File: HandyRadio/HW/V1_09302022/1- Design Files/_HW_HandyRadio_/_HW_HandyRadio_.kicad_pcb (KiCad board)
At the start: 4 copper layers, 74.9 x 74.9 mm, 170 parts, among them J1 MHDR_4POS_1ROW, J2 RECEP_6POS_1ROW, J3 XH_CONN_2POS_R/A, J4 USB_uAB_RECEP, J5 XH_CONN_2POS_R/A, J6 MHDR_2POS_VERT, K1 DPDT_RELAY, Q1 IRF7401TRPBF, Q2 MMUN2215LT1G, SW1 SPST_NO_RA, SW2 SPST_NO_RA, SW3 SPST_NO_RA, U1 PIC16F15223, U2 IR_REC_38KHz, U3 PAM8302AASCR, U4 MCP73831, U5 AP7361EA, U6 R1211N002B, U7 MIC5365-3.3, U8 EGUARD0502A, U9 SI4735-D60-GU

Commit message: IT'S ALMOST GOOD FOR RELEASE, schematic should be checked and a double check on routing
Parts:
- H2, H3, H4, H5: footprint MountingHole:MountingHole_3.2mm_M3 -> _HW_HandyRadio_Footprint:MountingHole_3.2mm_M3
- moved H4 3.80 mm to (250.2, 176.4)
- moved H5 3.43 mm to (183.3, 176.5)
- moved H3 3.43 mm to (250.6, 109.2)
- moved H2 3.41 mm to (183.3, 109.2)
- moved R37 0.66 mm to (240.4, 137.2)
- moved R2 0.63 mm to (250.6, 121.6)
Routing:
- net GND: track 198.4 -> 206.7 mm
- net /BLOCK DIAGRAM/MCU, RTC, OLED, PB, LED/BATT_STAT: track 79.1 -> 87.2 mm
- net /BLOCK DIAGRAM/MCU, RTC, OLED, PB, LED/PB_1: track 37.2 -> 45.2 mm
- net /BLOCK DIAGRAM/MCU, RTC, OLED, PB, LED/~{FM}/SW_SEL: track 47.0 -> 51.5 mm
- net /BLOCK DIAGRAM/MCU, RTC, OLED, PB, LED/IR_INPUT: track 49.7 -> 52.7 mm
- net /BLOCK DIAGRAM/MCU, RTC, OLED, PB, LED/ICSPCLK: track 76.8 -> 75.8 mm
- net Net-(J1-Pad4): track 3.11 -> 3.75 mm
- added copper zone on B.Cu, net GND
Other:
- board text added: "! DO NOT TOUCH !"
- board text added: "(C) 2022 Siavash Taher Parvar ALL RIGHTS RESERVED"
- board text added: "+ -"
- board text added: "+3.7V BATT"
- board text added: "+SPK -SPK"
- board text added: "8OHM SPK"
- board text added: "@Mend0z0"
- board text added: "AM ANT"
- board text added: "GND ICSPCLK ICSPDAT VCC"
- board text added: "Handy Radio Supported band AM/FM/SW/LW"
- board text added: "IR GND VCC"
- board text added: "M3"
- board text added: "Released Date: Nov 2nd, 2022"
- board text added: "To my professors that I liked to present this project while they were alive. GOD BLESS YOU, RIP! Prof. Nina Jagaric (RF Class) Prof. Kam Pui Tang (MCU Class) Fall 2022, Centennial College"
- board text added: "Version/Revsion: V1I1"
- board text added: "X RST SDA SCL +3V3 GND"

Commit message: some modification
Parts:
- removed DIS1: OLED, _HW_HandyRadio_Footprint:OLED 1.3INCH
- added DIS601: OLED, _HW_HandyRadio_Footprint:OLED 1.3INCH, F.Cu at (202.7, 126.1)
- added R512: 16K5R, Resistor_SMD:R_0805_2012Metric_Pad1.20x1.40mm_HandSolder, F.Cu at (173.2, 145.3)
- added REF**: Logo, _HW_HandyRadio_Footprint:Logo, F.Cu at (239.6, 124.7)
- added TP506: TPC, TestPoint:TestPoint_Pad_D1.5mm, F.Cu at (169.3, 138.0)
- renumbered ANT2 to ANT801, C1 to C301, C2 to C302, C3 to C303, C4 to C304, C5 to C305, C6 to C306, C7 to C307, C8 to C308, C9 to C309, C10 to C310, C11 to C311, C12 to C312, C13 to C313, C14 to C314, C15 to C315, C16 to C316, C17 to C401, C18 to C402, C19 to C403, C20 to C404, C21 to C405, C22 to C406, C23 to C407, C24 to C501, C25 to C502, C26 to C503, C27 to C504, C28 to C505, C29 to C506, C30 to C507, C31 to C508, C32 to C509, C33 to C510, C34 to C511, C35 to C512, C36 to C513, C37 to C514, C38 to C515, C39 to C516, C40 to C517, C41 to C518, C42 to C519, C43 to C520, C44 to C521, C45 to C522, C46 to C523, C47 to C524, C48 to C525, C49 to C526, C50 to C527, C51 to C528, C52 to C801, C53 to C802, C54 to C803, C55 to C804, C56 to C805, C57 to C806, C58 to C807, C59 to C808, C60 to C809, C61 to C810, C62 to C811, C63 to C812, C64 to C813, C65 to C814, C66 to C815, C67 to C816, C68 to C817, C69 to C818, C70 to C819, D1 to D301, D2 to D501, EC1 to EC501, EC2 to EC502, EC3 to EC503, EC4 to EC801, EC5 to EC802, EC6 to EC803, H2 to H602, H3 to H603, H4 to H604, H5 to H605, J1 to J301, J2 to J302, J3 to J401, J4 to J501, J5 to J502, J6 to J801, K1 to K801, L1 to L501, L2 to L801, L3 to L802, L4 to L803, L5 to L804, Q1 to Q501, Q2 to Q801, R1 to R301, R2 to R302, R3 to R303, R4 to R304, R5 to R305, R6 to R306, R7 to R307, R8 to R308, R9 to R309, R10 to R310, R11 to R311, R12 to R312, R13 to R313, R14 to R314, R15 to R315, R16 to R316, R17 to R401, R18 to R402, R19 to R403, R20 to R501, R21 to R502, R22 to R503, R23 to R504, R24 to R505, R25 to R506, R26 to R507, R27 to R508, R28 to R509, R29 to R510, R30 to R511, R32 to R801, R33 to R802, R34 to R803, R35 to R804, R36 to R805, R37 to R806, R38 to R807, R39 to R808, SW1 to SW301, SW2 to SW302, SW3 to SW303, TP1 to TP301, TP2 to TP302, TP3 to TP303, TP4 to TP304, TP5 to TP305, TP6 to TP306, TP7 to TP307, TP8 to TP308, TP9 to TP309, TP10 to TP310, TP11 to TP501, TP12 to TP502, TP13 to TP503, TP14 to TP504, TP15 to TP505, TP17 to TP507, TP18 to TP508, TP19 to TP509, TP20 to TP801, TP21 to TP802, U1 to U301, U2 to U302, U3 to U401, U4 to U501, U5 to U502, U6 to U503, U7 to U504, U8 to U801, U9 to U802
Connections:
- C521 pad 1: Net-(C44-Pad1) -> Net-(C521-Pad1)
- R506 pad 2: Net-(C44-Pad1) -> Net-(C521-Pad1)
- R508 pad 2: Net-(C44-Pad1) -> Net-(C521-Pad1)
- R511 pad 1: Net-(C44-Pad1) -> Net-(C521-Pad1)
- TP505 pad 1: Net-(C44-Pad1) -> Net-(C521-Pad1)
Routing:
- net Net-(C521-Pad1): track 0.00 -> 17.7 mm, vias 0 -> 1
- net Net-(C44-Pad1): track 17.7 -> 0.00 mm, vias 1 -> 0
- net GND: track 206.7 -> 202.2 mm, vias 98 -> 96
- net +3V3: track 95.9 -> 97.8 mm
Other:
- board text removed: "@Mend0z0"

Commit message: Serious changes in placement
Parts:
- removed R31: 16KR5, Resistor_SMD:R_0805_2012Metric_Pad1.20x1.40mm_HandSolder
- C308, C313, C316, C401, C402, C403, C502, C503, C504, C505, C506, C510, C511, C512, C514, C517, C518, C519, C520, C522, C524, C801, C802, C803, C806, C807, C810, C813, C818, C819, EC801, EC802, EC803, Q801, R309, R310, R312, R314, R315, R316, R502, R505, R508, R509, R510, R807, R808: moved to F.Cu
- moved R512 28.0 mm to (197.0, 160.0), turned to 180 degrees
- moved TP506 27.1 mm to (196.1, 141.9)
- moved R807 25.5 mm to (247.8, 135.0), turned to 180 degrees
- moved R808 24.2 mm to (251.9, 135.0), turned to 0 degrees
- moved C819 18.4 mm to (247.8, 137.2), turned to 0 degrees
- moved C818 16.7 mm to (251.9, 137.2), turned to 180 degrees
- moved R510 12.3 mm to (201.9, 148.8)
- moved C313 11.7 mm to (220.4, 115.8), turned to 0 degrees
- moved R312 11.7 mm to (224.4, 115.8), turned to 180 degrees
- moved C807 11.6 mm to (230.6, 162.3), turned to 0 degrees
- moved Q801 10.8 mm to (226.3, 166.5), turned to 0 degrees
- moved C524 10.1 mm to (208.3, 113.9), turned to 180 degrees
- moved TP307 9.60 mm to (214.0, 175.3)
- moved TP310 9.60 mm to (214.0, 177.8)
- moved C403 9.28 mm to (201.1, 165.8), turned to 0 degrees
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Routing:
- net GND: track 202.2 -> 17.7 mm, vias 96 -> 11
- net +5V: track 65.5 -> 0.00 mm, vias 26 -> 0
- net +3V3: track 97.8 -> 33.6 mm, vias 30 -> 5
- net /BLOCK DIAGRAM/MCU, RTC, OLED, PB, LED/BATT_STAT: track 87.2 -> 54.3 mm, vias 2 -> 0
- net +6V: track 30.0 -> 0.00 mm, vias 13 -> 0
- net +BATT: track 24.5 -> 0.00 mm, vias 12 -> 3
- net /BLOCK DIAGRAM/RF RECEIVER/~{RST}: track 22.2 -> 0.00 mm
- net Net-(C809-Pad1): track 19.5 -> 0.00 mm, vias 2 -> 0
- net /BLOCK DIAGRAM/RF RECEIVER/~{SEN}: track 19.1 -> 0.00 mm
- net /BLOCK DIAGRAM/MCU, RTC, OLED, PB, LED/~{FM}/SW_SEL: track 51.5 -> 32.7 mm, vias 2 -> 1
- net Net-(R502-Pad2): track 18.5 -> 0.00 mm, vias 1 -> 0
- net Net-(C521-Pad1): track 17.7 -> 0.00 mm, vias 1 -> 0
- net /BLOCK DIAGRAM/RF RECEIVER/SCLK: track 16.9 -> 0.00 mm
- net /BLOCK DIAGRAM/MCU, RTC, OLED, PB, LED/SI47_CLK: track 28.8 -> 14.1 mm
- net /BLOCK DIAGRAM/RF RECEIVER/SDIO: track 14.3 -> 0.00 mm
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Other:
- board size 74.9 x 74.9 mm -> 75 x 75 mm
- board text removed: "M3"

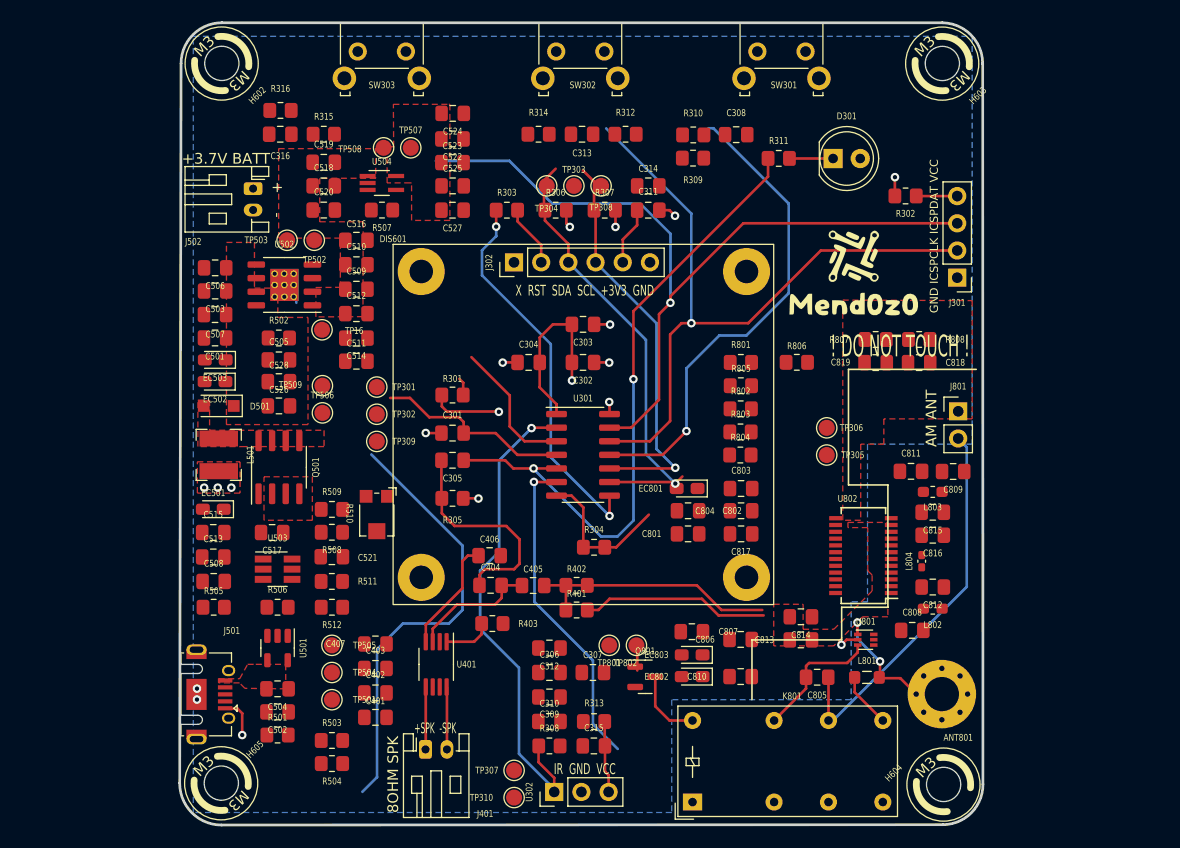
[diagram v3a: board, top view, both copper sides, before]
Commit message: replacement almost done, but routing left
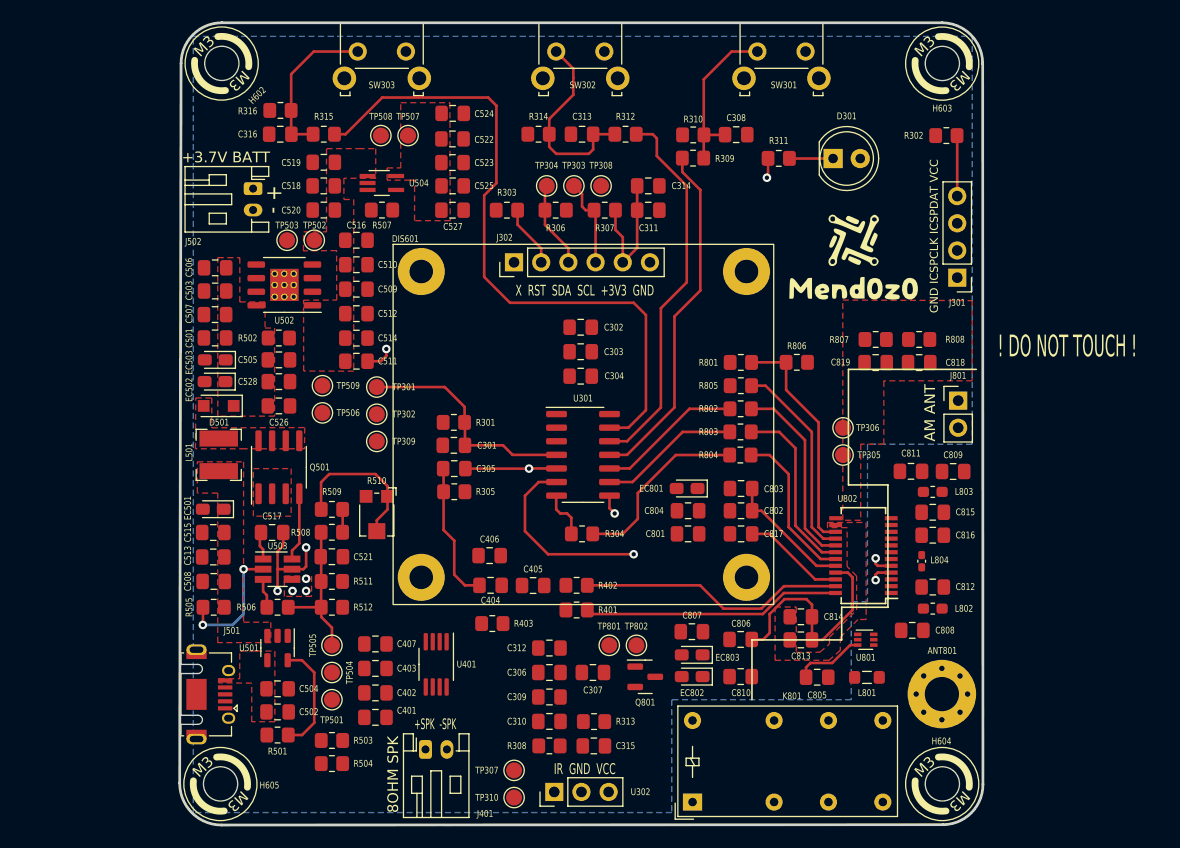
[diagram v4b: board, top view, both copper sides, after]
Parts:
- removed REF**: Logo, _HW_HandyRadio_Footprint:Logo
- removed TP16: TPC, TestPoint:TestPoint_Pad_D1.5mm
- added LBL602: Mend0z0_LOGO, _HW_HandyRadio_Footprint:Logo, F.Cu at (239.5, 123.2)
- moved R302 6.81 mm to (254.4, 116.0)
- moved C304 5.03 mm to (220.3, 138.4), turned to 180 degrees
- moved C302 3.29 mm to (220.3, 133.9)
- moved C303 2.57 mm to (220.3, 136.2)
- moved R301 2.56 mm to (208.4, 142.8)
- moved R304 1.68 mm to (220.4, 153.2)
- moved TP305 1.52 mm to (244.8, 145.8)
- moved TP306 1.52 mm to (244.8, 143.3)
- moved TP507 1.17 mm to (204.1, 116.0)
- moved TP508 1.17 mm to (201.6, 116.0)
- moved C301 1.15 mm to (208.4, 144.9)
- moved J801 1.00 mm to (255.5, 140.7)
- moved C305 0.80 mm to (208.4, 147.1)
- moved R305 0.64 mm to (208.4, 149.2)
- moved H604 0.13 mm to (251.6, 179.0)
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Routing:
- net /BLOCK DIAGRAM/MCU, RTC, OLED, PB, LED/BATT_STAT: track 54.3 -> 0.00 mm
- net /BLOCK DIAGRAM/MCU, RTC, OLED, PB, LED/LED_IND: track 60.7 -> 10.4 mm
- net /BLOCK DIAGRAM/MCU, RTC, OLED, PB, LED/IR_INPUT: track 46.1 -> 0.00 mm, vias 1 -> 0
- net Net-(C805-Pad1): track 36.4 -> 0.00 mm
- net Net-(R303-Pad1): track 35.9 -> 1.87 mm, vias 2 -> 1
- net /BLOCK DIAGRAM/MCU, RTC, OLED, PB, LED/ICSPCLK: track 66.0 -> 35.5 mm, vias 1 -> 0
- net /BLOCK DIAGRAM/RF RECEIVER/~{RST}: track 0.00 -> 21.7 mm
- net +5V: track 0.00 -> 21.5 mm
- net /BLOCK DIAGRAM/MCU, RTC, OLED, PB, LED/I2C_SDA: track 42.1 -> 21.3 mm, vias 1 -> 0
- net /BLOCK DIAGRAM/RF RECEIVER/~{SEN}: track 0.00 -> 19.0 mm
- net Net-(C313-Pad2): track 0.00 -> 18.5 mm
- net /BLOCK DIAGRAM/RF RECEIVER/SCLK: track 0.00 -> 18.0 mm
- net /BLOCK DIAGRAM/RF RECEIVER/SDIO: track 0.00 -> 16.8 mm
- net /BLOCK DIAGRAM/MCU, RTC, OLED, PB, LED/I2C_SCL: track 37.6 -> 22.0 mm, vias 1 -> 0
- net Net-(C308-Pad2): track 0.00 -> 15.4 mm
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
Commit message: routing on progress
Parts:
- moved C316 43.3 mm to (235.2, 120.7), turned to 180 degrees
- moved R315 35.4 mm to (231.3, 120.7), turned to 180 degrees
- moved C308 19.1 mm to (235.2, 135.0)
- moved R309 16.9 mm to (231.3, 135.0)
- moved C313 16.5 mm to (235.2, 123.0), turned to 180 degrees
- moved R312 9.88 mm to (231.3, 123.0), turned to 0 degrees
- moved R310 8.47 mm to (239.2, 115.2)
- moved R311 4.85 mm to (239.3, 122.9)
- moved R316 4.31 mm to (196.3, 115.1), turned to 0 degrees
- moved R314 4.15 mm to (220.4, 115.1)
- moved C809 3.07 mm to (253.1, 144.9), turned to 0 degrees
- moved TP305 2.95 mm to (244.8, 142.9), turned to -90 degrees
- moved TP306 2.13 mm to (244.8, 145.4), turned to -90 degrees
- moved C811 2.04 mm to (253.1, 147.1)
- moved U504 0.87 mm to (201.7, 119.5)
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- renumbered EC501 to TC501, EC502 to TC502, EC503 to TC503, EC801 to TC801, EC802 to TC802, EC803 to TC803
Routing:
- net Net-(C805-Pad1): track 0.00 -> 38.9 mm
- net Net-(C316-Pad2): track 14.7 -> 52.4 mm, vias 0 -> 1
- net Net-(C308-Pad2): track 15.4 -> 49.8 mm
- net GND: track 12.8 -> 45.4 mm, vias 3 -> 29
- net +3V3: track 24.9 -> 50.8 mm, vias 0 -> 24
- net Net-(C809-Pad1): track 0.00 -> 23.7 mm, vias 0 -> 2
- net Net-(C313-Pad2): track 18.5 -> 41.2 mm, vias 0 -> 1
- net /BLOCK DIAGRAM/MCU, RTC, OLED, PB, LED/ICSPCLK: track 35.5 -> 56.1 mm, vias 0 -> 1
- net /BLOCK DIAGRAM/MCU, RTC, OLED, PB, LED/PB_1: track 32.9 -> 14.8 mm
- net Net-(ANT801-Pad1): track 0.00 -> 16.9 mm, vias 0 -> 1
- net /BLOCK DIAGRAM/MCU, RTC, OLED, PB, LED/BATT_STAT: track 0.00 -> 14.3 mm
- net Net-(C404-Pad2): track 0.00 -> 12.2 mm
- net Net-(C406-Pad2): track 0.00 -> 10.7 mm
- net /BLOCK DIAGRAM/MCU, RTC, OLED, PB, LED/IR_INPUT: track 0.00 -> 8.87 mm
- net /BLOCK DIAGRAM/MCU, RTC, OLED, PB, LED/~{FM}/SW_SEL: track 17.8 -> 26.6 mm, vias 1 -> 2
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- added copper zone on B.Cu, net +3V3
- added copper zone on B.Cu, net +5V
- added copper zone on B.Cu, net +BATT
- added copper zone on In2.Cu, net GND
- removed copper zone on In2.Cu, net +3V3
- removed copper zone on In2.Cu, net +5V
- removed copper zone on In2.Cu, net +6V
- removed copper zone on In2.Cu, net +BATT
- removed copper zone on B.Cu, net GND
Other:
- board text added: "Handy Radio Supported bands AM/FM/SW/LW"
- board text removed: "Handy Radio Supported band AM/FM/SW/LW"

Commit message: routing has been almost done
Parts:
- moved R402 2.82 mm to (220.4, 155.2)
- moved R401 2.34 mm to (220.4, 158.0)
- moved TP301 1.14 mm to (201.2, 140.6)
- moved TP302 1.14 mm to (201.2, 143.1)
- moved TP309 1.14 mm to (201.2, 145.7)
- moved SW301 0.52 mm to (239.2, 110.3)
- moved SW302 0.52 mm to (220.4, 110.3)
- moved SW303 0.52 mm to (201.9, 110.3)
- moved TP501 0.10 mm to (197.1, 168.7)
- moved TP504 0.10 mm to (197.1, 166.1)
- moved TP505 0.10 mm to (197.1, 163.6)
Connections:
- R304 pad 1: /BLOCK DIAGRAM/MCU, RTC, OLED, PB, LED/SI47_CLK -> Net-(R304-Pad1)
- U301 pad 7: /BLOCK DIAGRAM/MCU, RTC, OLED, PB, LED/SI47_CLK -> Net-(R304-Pad1)
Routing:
- net /BLOCK DIAGRAM/MCU, RTC, OLED, PB, LED/IR_INPUT: track 8.87 -> 86.5 mm, vias 0 -> 1
- net GND: track 45.4 -> 106.1 mm, vias 29 -> 62
- net /BLOCK DIAGRAM/MCU, RTC, OLED, PB, LED/LED_IND: track 8.52 -> 68.3 mm, vias 1 -> 2
- net /BLOCK DIAGRAM/MCU, RTC, OLED, PB, LED/BATT_STAT: track 14.3 -> 63.4 mm, vias 0 -> 2
- net Net-(R303-Pad1): track 1.87 -> 35.3 mm, vias 1 -> 2
- net +6V: track 0.00 -> 31.8 mm, vias 0 -> 2
- net /BLOCK DIAGRAM/RF RECEIVER/GPO2: track 2.04 -> 31.5 mm, vias 1 -> 2
- net /BLOCK DIAGRAM/RF RECEIVER/GPO1: track 2.04 -> 28.6 mm, vias 1 -> 2
- net +BATT: track 4.61 -> 28.7 mm, vias 13 -> 15
- net /BLOCK DIAGRAM/MCU, RTC, OLED, PB, LED/SI47_CLK: track 21.8 -> 35.6 mm, vias 0 -> 2
- net Net-(R304-Pad1): track 0.00 -> 4.77 mm
- net /BLOCK DIAGRAM/DCDC PWS/PROG: track 10.4 -> 15.1 mm, vias 0 -> 2
- net /BLOCK DIAGRAM/MCU, RTC, OLED, PB, LED/ICSPDAT: track 57.3 -> 60.8 mm
- net Net-(C308-Pad2): track 49.8 -> 47.8 mm
- net /BLOCK DIAGRAM/MCU, RTC, OLED, PB, LED/~{FM}/SW_SEL: track 26.6 -> 24.7 mm
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
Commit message: routing has finished
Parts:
- moved R510 0.51 mm to (201.4, 148.8)
- moved J501 0.10 mm to (188.1, 163.1)
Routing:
- net GND: track 106.1 -> 149.6 mm, vias 62 -> 73
- net /BLOCK DIAGRAM/MCU, RTC, OLED, PB, LED/I2C_SCL: track 22.0 -> 54.9 mm, vias 0 -> 1
- net /BLOCK DIAGRAM/MCU, RTC, OLED, PB, LED/I2C_SDA: track 21.3 -> 52.7 mm, vias 0 -> 1
- net Net-(R303-Pad1): track 35.3 -> 36.0 mm
- net /BLOCK DIAGRAM/MCU, RTC, OLED, PB, LED/LED_IND: track 68.3 -> 67.8 mm
- net Net-(R509-Pad1): track 14.4 -> 13.9 mm
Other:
- outline, holes or cut-outs redrawn

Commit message: Ready to release the HW :smile:
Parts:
- moved J801 0.66 mm to (254.7, 141.3)
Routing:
- net Net-(R303-Pad1): track 36.0 -> 59.1 mm
- net /BLOCK DIAGRAM/MCU, RTC, OLED, PB, LED/I2C_SCL: track 54.9 -> 40.7 mm
- net /BLOCK DIAGRAM/MCU, RTC, OLED, PB, LED/I2C_SDA: track 52.7 -> 43.3 mm
- net /BLOCK DIAGRAM/MCU, RTC, OLED, PB, LED/ICSPCLK: track 57.8 -> 54.5 mm
- net /BLOCK DIAGRAM/MCU, RTC, OLED, PB, LED/ICSPDAT: track 60.8 -> 57.6 mm
- net Net-(C313-Pad2): track 40.9 -> 41.8 mm
- net Net-(C805-Pad1): track 38.9 -> 38.2 mm
- net Net-(C805-Pad2): track 11.9 -> 12.5 mm
- net GND: vias 73 -> 100
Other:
- board text added: "Handy Radio Supported broadbands AM/FM/SW/LW"
- board text added: "Released Date: 11/11/2022"
- board text added: "To my professors that I liked to present this project while they were alive. GOD BLESS YOU, RIP! Professor Nina Jagaric (RF Class) Professor Kam Pui Tang (MCU Class) Fall 2022, Centennial College"
- board text removed: "Handy Radio Supported bands AM/FM/SW/LW"
- board text removed: "Released Date: Nov 2nd, 2022"
- board text removed: "To my professors that I liked to present this project while they were alive. GOD BLESS YOU, RIP! Prof. Nina Jagaric (RF Class) Prof. Kam Pui Tang (MCU Class) Fall 2022, Centennial College"
